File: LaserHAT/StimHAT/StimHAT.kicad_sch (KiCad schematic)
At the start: 112 parts, among them J1 GPIO, J10 OLED 0.91 (GND VCC SCL SDA), J101 ELECTRODE E1/E2, J102 B4B-PH-K-S(LF)(SN), J103 5V TO DC-DC POD, J5 GT-USB-7010ASV, J6 BNC TRIGGER IN, J7 BNC STIM OUT, Q3 AP30P30Q, Q4 DMMT5401, Q5 AP30P30Q, SW10 MSK12C02, SW6 TS-1088-AR02016, SW7 SKRHADE010, SW9 TS-1088-AR02016, U1 M24C32-WDW6TP, U101 ISO7741FDBQR, U104 TLV76050DBZR, U105 DAC60501ZDGSR, U106 OPA2192IDGKR, U107 CD74HC4053PWR, U108 DG418DY-T1-E3, U109 ISO1640BDR, U110 TLV1702AIDGKR, U4 MCP1700T-3302E/MB, U5 AP2171W, U6 CH340N, U7 MSPM0G1507SRHBR, U8 74LVC2G17GW

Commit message: StimHAT: joystick fan re-laid on an even pitch, 3D models, routing clean-up
Joystick fan: six 45-degree diagonals at a 1.0 mm x+y pitch (0.5 mm copper gap), rows 0.6 mm
apart under U7's south pins, verticals 0.7 mm apart; BUTTON4 is one straight line from its
back-side via to pad 6.  MCU_STIM_OUT's via moved out of pin 20's column, BSL_INVOKE straight
down into SW6, U8.2's ground stitched by a new via (the old one clashed with the STIM_OUT via).

3D models: generated VRML for the ALPS joystick, TI's RHB VQFN-32 on U7, Q3 / Q5 / SW10 paths
pointed at the shared ../Footprints.3dshapes.  "USB" silk moved out of U6's outline.

Generators follow the user's hand edits (LED on pin 9 / PA5, TP102); the regenerated netlist
matches the pushed schematic exactly.  DRC 0 errors / 0 warnings, 0 open connections.

Co-Authored-By: Claude Fable 5.1 <noreply@anthropic.com>
Claude-Session: https://claude.ai/code/session_015kiXLxnPpBaXdXJu2EMvn7
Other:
- note added: "down PA15, centre PA14, left PA12 (BACK), right PA13 (BUTTON6); FIRE SW9 PA16; LED PA5; all active low. J10: unpopulated socket for a 0.91 in I2C OLED instead of the bonnet."
- note removed: "down PA15, centre PA14, left PA12 (BACK), right PA13 (BUTTON6); FIRE SW9 PA16; LED PA6; all active low. J10: unpopulated socket for a 0.91 in I2C OLED instead of the bonnet."

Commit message: StimHAT: pre-order audit round 1 fixes
Four independent reviews (schematic, parts/footprints/pinouts, layout/fab, LCSC/sync) of 4f280fb.
Blockers: the ALPS joystick land pattern (pads 0 / +-1.425 mm and bosses +-1.9 mm, not +-1.85 /
2.15) regenerated and swapped, fan tails and a pad-5 via follow; U8 -> SN74LVC2G17DCKR C50714
(C80500 out of stock).  Barrier: isolated SCL under U109 moved to y 20.68 and the notch made
structural (keep-out to y 20.55, C124 to (45.5, 21.8)); south strip 41.1-43.6 for J7's tails.
C17 back at U6, C127 added at U107's VCC pin, R3 4.7k, C12 1uF, U5B_IN -> U106B_IN, J102 "+V" /
"-V" front marks and 0.8 mm holes, six LCSC swaps to Basic/Preferred parts, stamp_fields clears
stale codes / excludes DNP from the CPL / skips board-only graphics, +5V In2 run 0.9 mm, stale
pin-map texts refreshed, BOM and fab outputs regenerated.  DRC 0 errors / 0 open, ERC 0,
path / sync 0.  Full write-up in README "Pre-order audit round 1".

Co-Authored-By: Claude Fable 5.1 <noreply@anthropic.com>
Claude-Session: https://claude.ai/code/session_015kiXLxnPpBaXdXJu2EMvn7
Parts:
- added C127: 100nF, Capacitor_SMD:C_0402_1005Metric, symbol stimhat:C
- C111, C112: LCSC Part # C559769 -> C5199872
- C12: value 100nF -> 1uF; LCSC Part # C307331 -> C52923
- C121: LCSC Part # C726584 -> C28323
- D101: LCSC Part # C124205 -> C7502694
- D103, D104: LCSC Part # C173445 -> C19077451
- R115: LCSC Part # C137973 -> C25118
- R3: value 10k -> 4.7k; LCSC Part # C25744 -> C25900
- R4: LCSC Part # C844674 -> C852472
- U8: value 74LVC2G17GW -> SN74LVC2G17DCKR; LCSC Part # C80500 -> C50714
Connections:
- net +5V_ISO: now also C127.1
- net GND_ISO: now also C127.2
- net U5B_IN renamed U106B_IN
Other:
- note added: "J6 -> R23 1k / R24 100k -> U8A -> PA21 (TIMG8 capture). PA17 -> U8B -> R25 33 -> J7, D9 mirrors the pulses. C16 (2.6 mm away) bypasses U8."
- note added: "Module lines (U7 pins 26-31, U101's order): PA22 FAULT_H, PA23 CATH_H, PA24 EN_H, PA25 RELEASE_H, PA26 SDA_H, PA27 SCL_H. Joystick SW7 (SKRHADE010, mounted at 135 deg): up PA7,"
- note added: "Pi header: 3.3 V (pins 1/17) feeds the ID EEPROM and the I2C pull-ups; 5 V (2/4) the LDO U4. GPIO9 (pin 21) = NRST, GPIO10 (pin 19) = MCU power"
- note added: "enable, GPIO18 (pin 12) = trigger, GPIO24/25 = SWD, GPIO14/15 = UART; GPIO 4/5/6/17/22/23/27 (the bonnet's buttons) stay free. No SPI0 / I2S / PWM-on-18 overlays."
- note removed: "J6 -> R23 1k / R24 100k -> U8A -> PA26 (TIMG8 capture). PA25 (TIMG12) -> U8B -> R25 33 -> J7, D9 mirrors the pulses."
- note removed: "Module lines from the Rev 2 J8 / J9 pins: PA6 FAULT_H, PA7 EN_H, PA12 CATH_H, PA15 RELEASE_H, PA17 SDA_H, PA22 SCL_H (StimHAT: see the README's pin map). Joystick SW7 (SKRHADE010, mounted at 135 deg): up PA7,"
- note removed: "Pi header: 3.3 V (pins 1/17) feeds the ID EEPROM and the I2C pull-ups; 5 V (2/4) the LDO U4. GPIO16 (pin 36) = NRST (was GPIO23:"
- note removed: "the Adafruit 4567 bonnet's joystick-right grounds GPIO23). GPIO18 = MCU power enable, GPIO24/25 = SWD, GPIO26 = trigger, GPIO14/15 = UART."

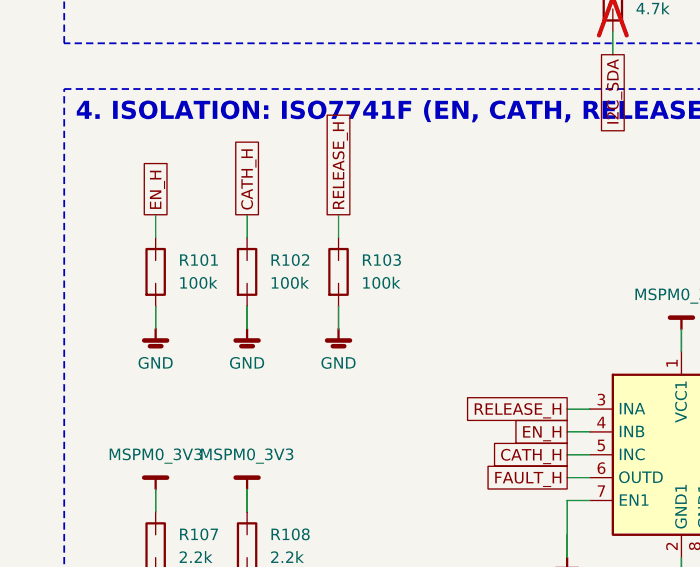
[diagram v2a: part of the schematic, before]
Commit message: StimHAT: pre-order audit round 2 fixes
Barrier at U104's GND_ISO pad back to >= 2.50 mm (HAT pour corner east of x 46.5 steps to y 43.7),
U109.8's via out of the pad, four via pairs beside U7 spread to JLC's 0.5 mm hole-to-hole, owl eye
pads re-attached to GND (stamp_fields keeps them), R101-R103 10k (ISO7741 leakage vs VIL), C111/C112
on a Basic code, parts-table tidy, README facts and round-2 section (pod-vs-bonnet depth is the open
user decision).  DRC 0 / 0 unconnected, ERC 0, BOM 50 lines, CPL 95.

Co-Authored-By: Claude Fable 5.1 <noreply@anthropic.com>
Claude-Session: https://claude.ai/code/session_015kiXLxnPpBaXdXJu2EMvn7
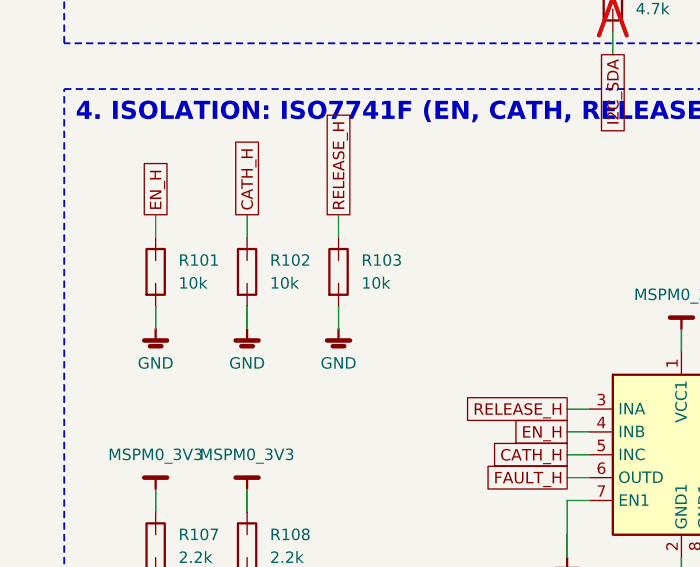
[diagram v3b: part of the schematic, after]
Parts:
- C111, C112: LCSC Part # C5199872 -> C15849
- R101, R102, R103: value 100k -> 10k; LCSC Part # C25741 -> C25744
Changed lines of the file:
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@@
   (symbol (lib_id "stimhat:R") (at 25.4 182.88 0) (unit 1) (exclude_from_sim no) (in_bom yes) (on_board yes) (dnp no)
     (property "Reference" "R101" (at 27.94 181.61  0) (effects (font (size 1.27 1.27)) (justify left)))
-    (property "Value" "100k" (at 27.94 184.15  0) (effects (font (size 1.27 1.27)) (justify left)))
+    (property "Value" "10k" (at 27.94 184.15  0) (effects (font (size 1.27 1.27)) (justify left)))
     (property "Footprint" "Resistor_SMD:R_0402_1005Metric" (at 25.4 182.88 0) (effects (font (size 1.27 1.27)) (hide yes)))
     (property "Datasheet" "" (at 25.4 182.88 0) (effects (font (size 1.27 1.27)) (hide yes)))
-    (property "LCSC Part #" "C25741" (at 25.4 182.88 0) (effects (font (size 1.27 1.27)) (hide yes)))
+    (property "LCSC Part #" "C25744" (at 25.4 182.88 0) (effects (font (size 1.27 1.27)) (hide yes)))
     (pin "1")
     (pin "2")
@@
   (symbol (lib_id "stimhat:R") (at 35.56 182.88 0) (unit 1) (exclude_from_sim no) (in_bom yes) (on_board yes) (dnp no)
     (property "Reference" "R102" (at 38.1 181.61  0) (effects (font (size 1.27 1.27)) (justify left)))
-    (property "Value" "100k" (at 38.1 184.15  0) (effects (font (size 1.27 1.27)) (justify left)))
+    (property "Value" "10k" (at 38.1 184.15  0) (effects (font (size 1.27 1.27)) (justify left)))
     (property "Footprint" "Resistor_SMD:R_0402_1005Metric" (at 35.56 182.88 0) (effects (font (size 1.27 1.27)) (hide yes)))
     (property "Datasheet" "" (at 35.56 182.88 0) (effects (font (size 1.27 1.27)) (hide yes)))
-    (property "LCSC Part #" "C25741" (at 35.56 182.88 0) (effects (font (size 1.27 1.27)) (hide yes)))
+    (property "LCSC Part #" "C25744" (at 35.56 182.88 0) (effects (font (size 1.27 1.27)) (hide yes)))
     (pin "1")
     (pin "2")
@@
   (symbol (lib_id "stimhat:R") (at 45.72 182.88 0) (unit 1) (exclude_from_sim no) (in_bom yes) (on_board yes) (dnp no)
     (property "Reference" "R103" (at 48.26 181.61  0) (effects (font (size 1.27 1.27)) (justify left)))
-    (property "Value" "100k" (at 48.26 184.15  0) (effects (font (size 1.27 1.27)) (justify left)))
+    (property "Value" "10k" (at 48.26 184.15  0) (effects (font (size 1.27 1.27)) (justify left)))
     (property "Footprint" "Resistor_SMD:R_0402_1005Metric" (at 45.72 182.88 0) (effects (font (size 1.27 1.27)) (hide yes)))
     (property "Datasheet" "" (at 45.72 182.88 0) (effects (font (size 1.27 1.27)) (hide yes)))
-    (property "LCSC Part #" "C25741" (at 45.72 182.88 0) (effects (font (size 1.27 1.27)) (hide yes)))
+    (property "LCSC Part #" "C25744" (at 45.72 182.88 0) (effects (font (size 1.27 1.27)) (hide yes)))
     (pin "1")
     (pin "2")
@@
     (property "Footprint" "Capacitor_SMD:C_0603_1608Metric" (at 208.28 269.24 0) (effects (font (size 1.27 1.27)) (hide yes)))
     (property "Datasheet" "" (at 208.28 269.24 0) (effects (font (size 1.27 1.27)) (hide yes)))
-    (property "LCSC Part #" "C5199872" (at 208.28 269.24 0) (effects (font (size 1.27 1.27)) (hide yes)))
+    (property "LCSC Part #" "C15849" (at 208.28 269.24 0) (effects (font (size 1.27 1.27)) (hide yes)))
     (pin "1")
     (pin "2")
@@
     (property "Footprint" "Capacitor_SMD:C_0603_1608Metric" (at 223.52 269.24 0) (effects (font (size 1.27 1.27)) (hide yes)))
     (property "Datasheet" "" (at 223.52 269.24 0) (effects (font (size 1.27 1.27)) (hide yes)))
-    (property "LCSC Part #" "C5199872" (at 223.52 269.24 0) (effects (font (size 1.27 1.27)) (hide yes)))
-    (pin "1")
-    (pin "2")
+    (property "LCSC Part #" "C15849" (at 223.52 269.24 0) (effects (font (size 1.27 1.27)) (hide yes)))
+    (pin "1")
+    (pin "2")
